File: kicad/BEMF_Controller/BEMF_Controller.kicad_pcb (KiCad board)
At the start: 2 copper layers, 164 parts, among them J1 HEADER4VALULOK, J2 HEADER6, J3 FUSE, J4 Coil_A, J5 Coil_B, J6 Coil_C, J7 Vin, Q1 C3M0280090D, Q2 C3M0280090D, Q3 C3M0280090D, Q4 C3M0280090D, Q5 C3M0280090D, Q6 C3M0280090D, U1 RASPBERRY_PICO-NO_DEBUG, U2 INA181, U3 TC1240A, U4 V_REG_78XX, U5 DGD2304, U6 DGD2304, U7 DGD2304

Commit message: reverted pcb back to original
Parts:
- removed C10, C24, C25, C26, C27, C32, C33, C34, C35, C6, C7, C8: 470uF, main:CPOL-RADIAL-5MM-10MM
- removed C13, C21, C22, C23, C28, C29, C30, C31, C36, C37, C38, C39: 1uF, Capacitor_SMD:C_1812_4532Metric
- removed C40, C41, C42: 1nF/50V, Capacitor_SMD:C_1210_3225Metric
- removed D10, D11, D12, D13, D14, D15, D16, D17, D18, D19, D20, D21, D22, D23, D24, D25, D26, D27, D28, D29, D30, D31, D32, D33, D34, D35, D36, D37, D38, D39, D40, D41, D42, D43, D44, D45, D46, D5, D6, D7, D8, D9: FSV20150V, Package_TO_SOT_SMD:TO-277A
- removed D47, D48, D51, D52, D55, D56: BZT52-B75J, main:SOD-123
- removed D49, D50, D53, D54, D57, D58: 1N4148WS, Diode_SMD:D_SOD-323
- removed J4: Coil_A, TerminalBlock_Phoenix:TerminalBlock_Phoenix_MKDS-1,5-2-5.08_1x02_P5.08mm_Horizontal
- removed J5: Coil_B, TerminalBlock_Phoenix:TerminalBlock_Phoenix_MKDS-1,5-2-5.08_1x02_P5.08mm_Horizontal
- removed J6: Coil_C, TerminalBlock_Phoenix:TerminalBlock_Phoenix_MKDS-1,5-2-5.08_1x02_P5.08mm_Horizontal
- removed J7: Vin, TerminalBlock_Phoenix:TerminalBlock_Phoenix_MKDS-1,5-2-5.08_1x02_P5.08mm_Horizontal
- removed JP1, JP2, JP3, JP4, JP5, JP6, JP7: Jumper, Jumper:SolderJumper-2_P1.3mm_Open_RoundedPad1.0x1.5mm
- removed R20, R21, R22, R23, R24, R25: 10k, Resistor_SMD:R_1210_3225Metric
- C1, C11, C12, C14, C15, C16, C17, C18, C19, C2, C20, C3: footprint Capacitor_SMD:C_1812_4532Metric -> main:1206
- C9: footprint Capacitor_SMD:C_0805_2012Metric -> main:1206
- Q1, Q2, Q3, Q4, Q5, Q6: value C3M0280090D -> MOSFET-NCHANNELTO-220-FLAT; footprint Package_TO_SOT_THT:TO-247-3_Horizontal_TabDown -> main:TO-220-FLAT
- R14, R15, R16, R17, R18, R19: value 10 -> 22; footprint Resistor_THT:R_Axial_DIN0411_L9.9mm_D3.6mm_P15.24mm_Horizontal -> main:1206
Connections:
- net /OVP_A renamed Net-(U1-GP0-Pad1)
- net /OVP_B renamed Net-(U1-GP1-Pad2)
- net /OVP_C renamed Net-(U1-GP2-Pad4)
- C9 pad 1: Net-(C9-Pad1) -> /THROTTLE
- Q1 pad 2: Net-(D9-K) -> /V_RAW
- Q1 pad 3: /SHUNT+ -> /COM_A
- Q2 pad 2: /CAP_BANK_A -> /COM_A
- Q2 pad 3: /COM_A -> /SHUNT+
- Q3 pad 2: /CAP_BANK_B -> /V_RAW
- Q4 pad 2: Net-(D41-K) -> /COM_B
- Q5 pad 2: /CAP_BANK_C -> /V_RAW
- Q6 pad 2: Net-(D45-K) -> /COM_C
- R14 pad 1: Net-(Q2-G) -> /DRV_AH
- R14 pad 2: /DRV_AH -> Net-(Q1-G)
- R15 pad 1: Net-(Q1-G) -> /DRV_AL
- R15 pad 2: /DRV_AL -> Net-(Q2-G)
- R16 pad 1: Net-(Q3-G) -> /DRV_BH
- R16 pad 2: /DRV_BH -> Net-(Q3-G)
- R17 pad 1: Net-(Q4-G) -> /DRV_BL
- R17 pad 2: /DRV_BL -> Net-(Q4-G)
- R18 pad 1: Net-(Q5-G) -> /DRV_CH
- R18 pad 2: /DRV_CH -> Net-(Q5-G)
- R19 pad 1: Net-(Q6-G) -> /DRV_CL
- R19 pad 2: /DRV_CL -> Net-(Q6-G)
- R8 pad 2: Net-(C9-Pad1) -> /THROTTLE
- U4 pad IN: Net-(J7-Pin_1) -> /V_RAW
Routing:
- net Net-(Q2-G): track 0.00 -> 39.6 mm, vias 0 -> 1
- net Net-(D9-K): track 39.6 -> 0.00 mm, vias 1 -> 0

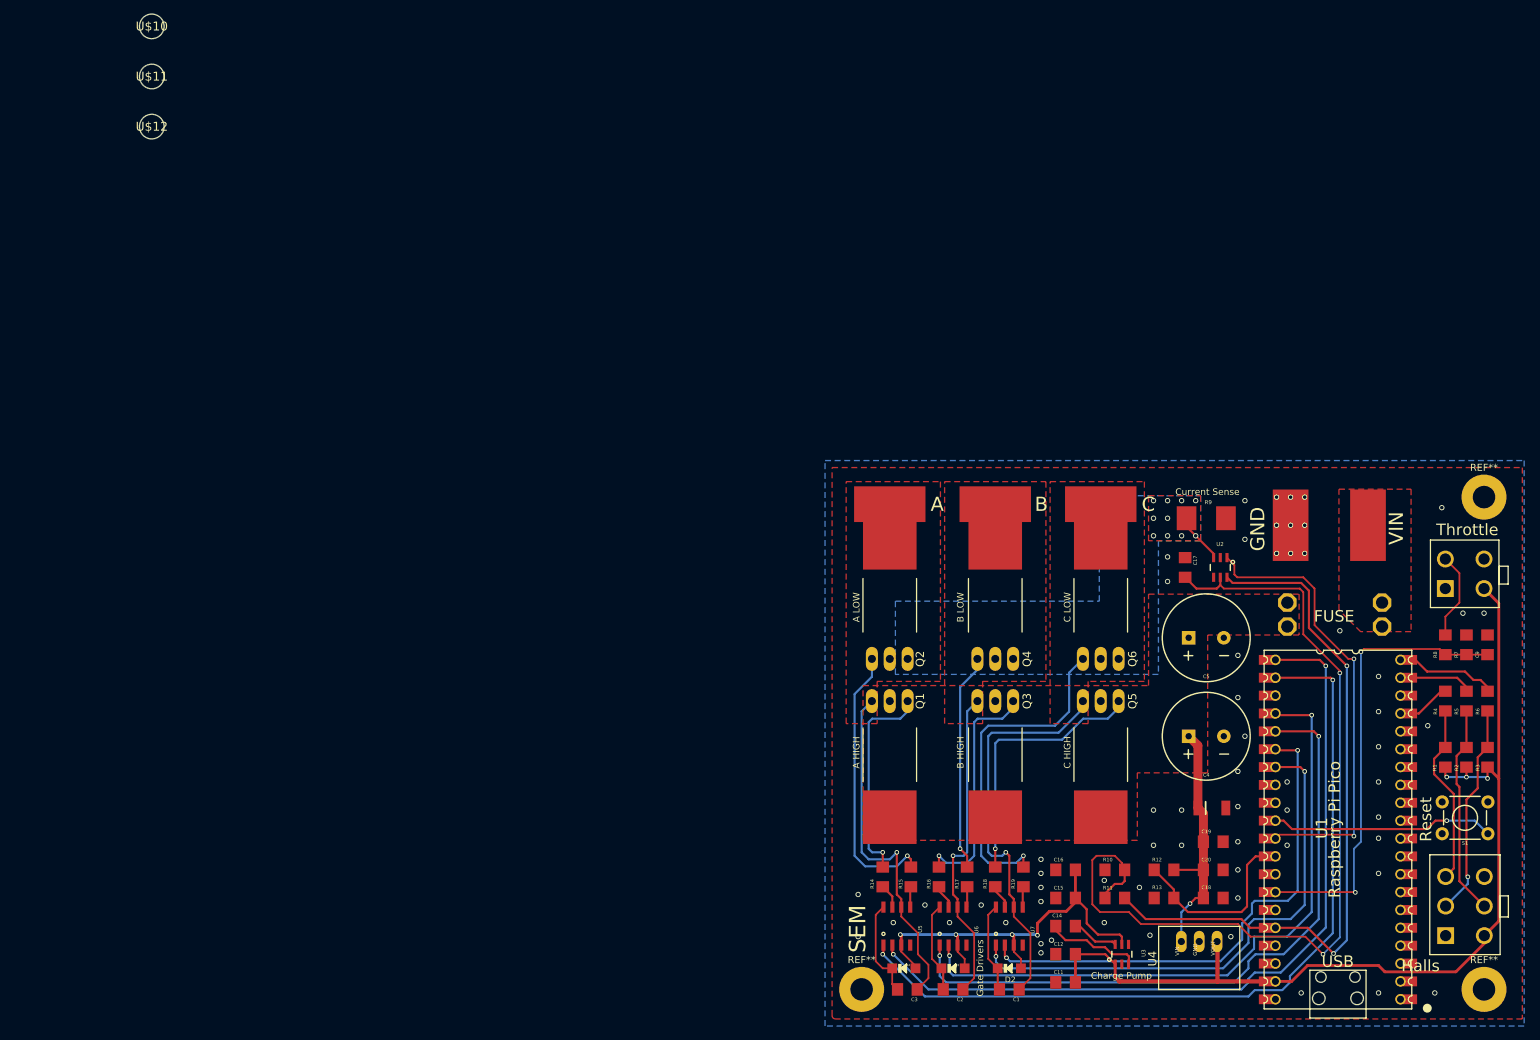
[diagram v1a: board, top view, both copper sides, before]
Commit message: Added component library
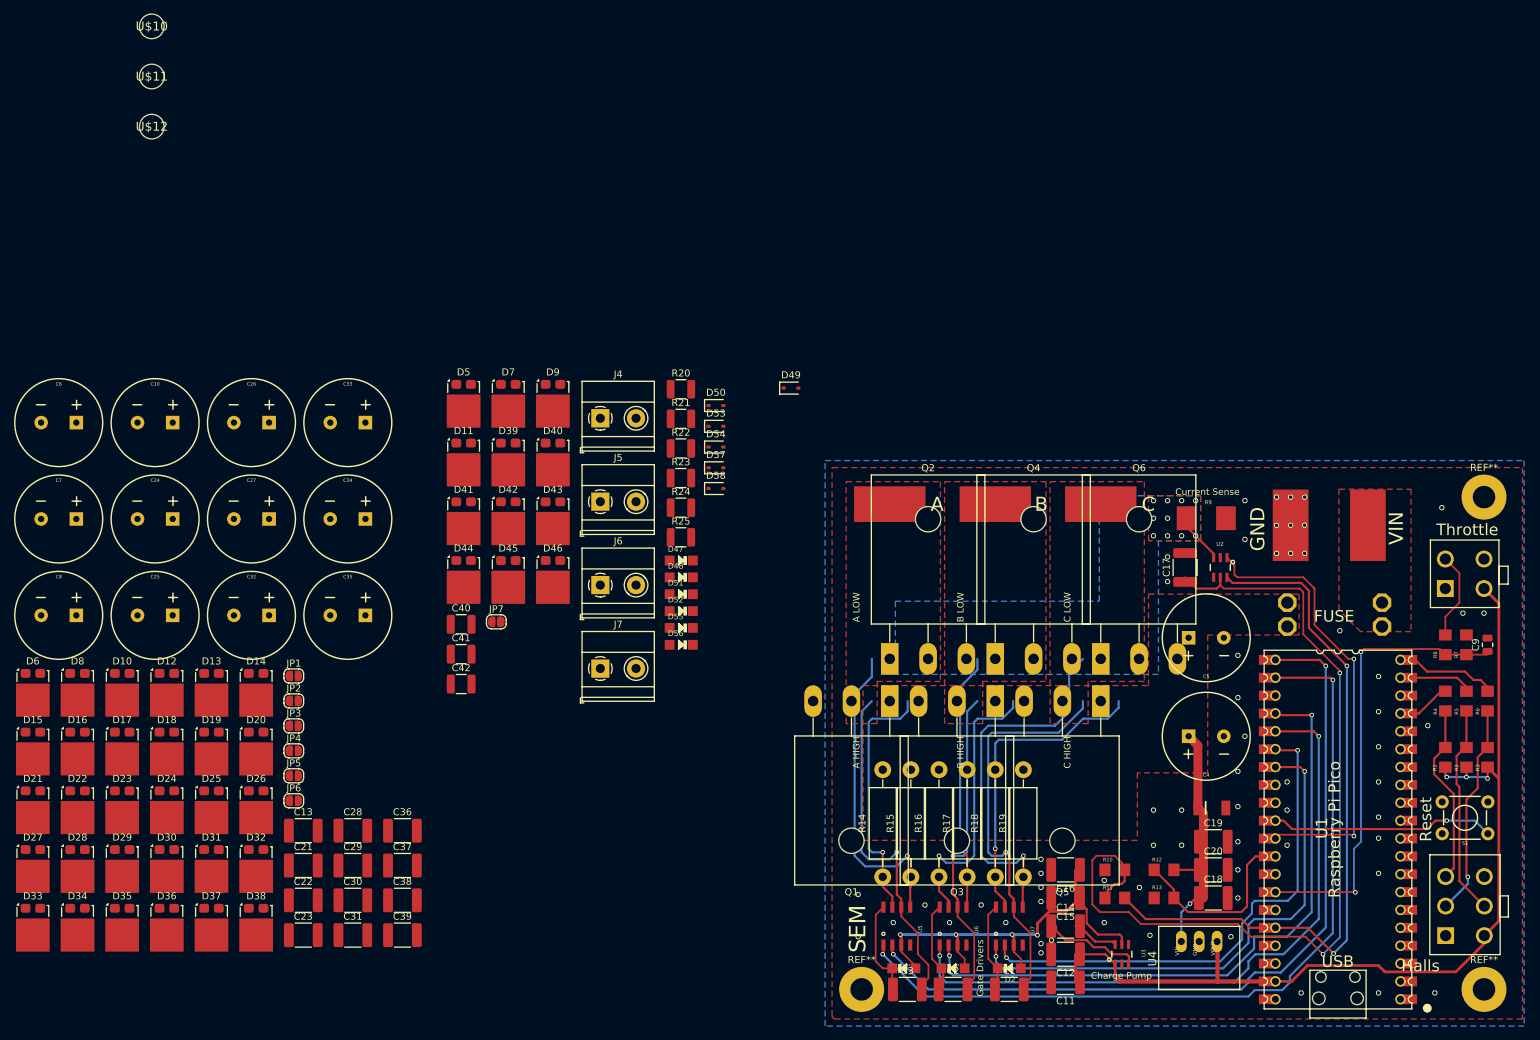
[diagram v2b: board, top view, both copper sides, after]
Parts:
- added C10: 470uF, main:CPOL-RADIAL-5MM-10MM, F.Cu at (3.53, 59.4)
- added C13: 1uF, Capacitor_SMD:C_1812_4532Metric, F.Cu at (24.6, 117.4)
- added C21: 1uF, Capacitor_SMD:C_1812_4532Metric, F.Cu at (24.6, 122.4)
- added C22: 1uF, Capacitor_SMD:C_1812_4532Metric, F.Cu at (24.6, 127.3)
- added C23: 1uF, Capacitor_SMD:C_1812_4532Metric, F.Cu at (24.6, 132.3)
- added C24: 470uF, main:CPOL-RADIAL-5MM-10MM, F.Cu at (3.53, 73.1)
- added C25: 470uF, main:CPOL-RADIAL-5MM-10MM, F.Cu at (3.53, 86.8)
- added C26: 470uF, main:CPOL-RADIAL-5MM-10MM, F.Cu at (17.2, 59.4)
- added C27: 470uF, main:CPOL-RADIAL-5MM-10MM, F.Cu at (17.2, 73.1)
- added C28: 1uF, Capacitor_SMD:C_1812_4532Metric, F.Cu at (31.7, 117.4)
- added C29: 1uF, Capacitor_SMD:C_1812_4532Metric, F.Cu at (31.7, 122.4)
- added C30: 1uF, Capacitor_SMD:C_1812_4532Metric, F.Cu at (31.7, 127.3)
- added C31: 1uF, Capacitor_SMD:C_1812_4532Metric, F.Cu at (31.7, 132.3)
- added C32: 470uF, main:CPOL-RADIAL-5MM-10MM, F.Cu at (17.2, 86.8)
- added C33: 470uF, main:CPOL-RADIAL-5MM-10MM, F.Cu at (30.9, 59.4)
- added C34: 470uF, main:CPOL-RADIAL-5MM-10MM, F.Cu at (30.9, 73.1)
- added C35: 470uF, main:CPOL-RADIAL-5MM-10MM, F.Cu at (30.9, 86.8)
- added C36: 1uF, Capacitor_SMD:C_1812_4532Metric, F.Cu at (38.7, 117.4)
- added C37: 1uF, Capacitor_SMD:C_1812_4532Metric, F.Cu at (38.7, 122.4)
- added C38: 1uF, Capacitor_SMD:C_1812_4532Metric, F.Cu at (38.7, 127.3)
- added C39: 1uF, Capacitor_SMD:C_1812_4532Metric, F.Cu at (38.7, 132.3)
- added C40: 1nF/50V, Capacitor_SMD:C_1210_3225Metric, F.Cu at (47.1, 88.1)
- added C41: 1nF/50V, Capacitor_SMD:C_1210_3225Metric, F.Cu at (47.1, 92.3)
- added C42: 1nF/50V, Capacitor_SMD:C_1210_3225Metric, F.Cu at (47.1, 96.6)
- added C6: 470uF, main:CPOL-RADIAL-5MM-10MM, F.Cu at (-10.2, 59.4)
- added C7: 470uF, main:CPOL-RADIAL-5MM-10MM, F.Cu at (-10.2, 73.1)
- added C8: 470uF, main:CPOL-RADIAL-5MM-10MM, F.Cu at (-10.2, 86.8)
- added D10: FSV20150V, Package_TO_SOT_SMD:TO-277A, F.Cu at (-1.15, 97.8)
- added D11: FSV20150V, Package_TO_SOT_SMD:TO-277A, F.Cu at (47.4, 65.1)
- added D12: FSV20150V, Package_TO_SOT_SMD:TO-277A, F.Cu at (5.20, 97.8)
- added D13: FSV20150V, Package_TO_SOT_SMD:TO-277A, F.Cu at (11.6, 97.8)
- added D14: FSV20150V, Package_TO_SOT_SMD:TO-277A, F.Cu at (17.9, 97.8)
- added D15: FSV20150V, Package_TO_SOT_SMD:TO-277A, F.Cu at (-13.8, 106.2)
- added D16: FSV20150V, Package_TO_SOT_SMD:TO-277A, F.Cu at (-7.50, 106.2)
- added D17: FSV20150V, Package_TO_SOT_SMD:TO-277A, F.Cu at (-1.15, 106.2)
- added D18: FSV20150V, Package_TO_SOT_SMD:TO-277A, F.Cu at (5.20, 106.2)
- added D19: FSV20150V, Package_TO_SOT_SMD:TO-277A, F.Cu at (11.6, 106.2)
- added D20: FSV20150V, Package_TO_SOT_SMD:TO-277A, F.Cu at (17.9, 106.2)
- added D21: FSV20150V, Package_TO_SOT_SMD:TO-277A, F.Cu at (-13.8, 114.5)
- added D22: FSV20150V, Package_TO_SOT_SMD:TO-277A, F.Cu at (-7.50, 114.5)
- added D23: FSV20150V, Package_TO_SOT_SMD:TO-277A, F.Cu at (-1.15, 114.5)
- added D24: FSV20150V, Package_TO_SOT_SMD:TO-277A, F.Cu at (5.20, 114.5)
- added D25: FSV20150V, Package_TO_SOT_SMD:TO-277A, F.Cu at (11.6, 114.5)
- added D26: FSV20150V, Package_TO_SOT_SMD:TO-277A, F.Cu at (17.9, 114.5)
- added D27: FSV20150V, Package_TO_SOT_SMD:TO-277A, F.Cu at (-13.8, 122.9)
- added D28: FSV20150V, Package_TO_SOT_SMD:TO-277A, F.Cu at (-7.50, 122.9)
- added D29: FSV20150V, Package_TO_SOT_SMD:TO-277A, F.Cu at (-1.15, 122.9)
- added D30: FSV20150V, Package_TO_SOT_SMD:TO-277A, F.Cu at (5.20, 122.9)
- added D31: FSV20150V, Package_TO_SOT_SMD:TO-277A, F.Cu at (11.6, 122.9)
- added D32: FSV20150V, Package_TO_SOT_SMD:TO-277A, F.Cu at (17.9, 122.9)
- added D33: FSV20150V, Package_TO_SOT_SMD:TO-277A, F.Cu at (-13.8, 131.2)
- added D34: FSV20150V, Package_TO_SOT_SMD:TO-277A, F.Cu at (-7.50, 131.2)
- added D35: FSV20150V, Package_TO_SOT_SMD:TO-277A, F.Cu at (-1.15, 131.2)
- added D36: FSV20150V, Package_TO_SOT_SMD:TO-277A, F.Cu at (5.20, 131.2)
- added D37: FSV20150V, Package_TO_SOT_SMD:TO-277A, F.Cu at (11.6, 131.2)
- added D38: FSV20150V, Package_TO_SOT_SMD:TO-277A, F.Cu at (17.9, 131.2)
- added D39: FSV20150V, Package_TO_SOT_SMD:TO-277A, F.Cu at (53.8, 65.1)
- added D40: FSV20150V, Package_TO_SOT_SMD:TO-277A, F.Cu at (60.1, 65.1)
- added D41: FSV20150V, Package_TO_SOT_SMD:TO-277A, F.Cu at (47.4, 73.4)
- added D42: FSV20150V, Package_TO_SOT_SMD:TO-277A, F.Cu at (53.8, 73.4)
- added D43: FSV20150V, Package_TO_SOT_SMD:TO-277A, F.Cu at (60.1, 73.4)
- added D44: FSV20150V, Package_TO_SOT_SMD:TO-277A, F.Cu at (47.4, 81.8)
- added D45: FSV20150V, Package_TO_SOT_SMD:TO-277A, F.Cu at (53.8, 81.8)
- added D46: FSV20150V, Package_TO_SOT_SMD:TO-277A, F.Cu at (60.1, 81.8)
- added D47: BZT52-B75J, main:SOD-123, F.Cu at (78.3, 79.0)
- added D48: BZT52-B75J, main:SOD-123, F.Cu at (78.3, 81.4)
- added D49: 1N4148WS, Diode_SMD:D_SOD-323, F.Cu at (94.0, 54.5)
- added D5: FSV20150V, Package_TO_SOT_SMD:TO-277A, F.Cu at (47.4, 56.7)
- added D50: 1N4148WS, Diode_SMD:D_SOD-323, F.Cu at (83.3, 57.0)
- added D51: BZT52-B75J, main:SOD-123, F.Cu at (78.3, 83.8)
- added D52: BZT52-B75J, main:SOD-123, F.Cu at (78.3, 86.2)
- added D53: 1N4148WS, Diode_SMD:D_SOD-323, F.Cu at (83.3, 59.9)
- added D54: 1N4148WS, Diode_SMD:D_SOD-323, F.Cu at (83.3, 62.9)
- added D55: BZT52-B75J, main:SOD-123, F.Cu at (78.3, 88.6)
- added D56: BZT52-B75J, main:SOD-123, F.Cu at (78.3, 91.0)
- added D57: 1N4148WS, Diode_SMD:D_SOD-323, F.Cu at (83.3, 65.8)
- added D58: 1N4148WS, Diode_SMD:D_SOD-323, F.Cu at (83.3, 68.8)
- added D6: FSV20150V, Package_TO_SOT_SMD:TO-277A, F.Cu at (-13.8, 97.8)
- added D7: FSV20150V, Package_TO_SOT_SMD:TO-277A, F.Cu at (53.8, 56.7)
- added D8: FSV20150V, Package_TO_SOT_SMD:TO-277A, F.Cu at (-7.50, 97.8)
- added D9: FSV20150V, Package_TO_SOT_SMD:TO-277A, F.Cu at (60.1, 56.7)
- added J4: Coil_A, TerminalBlock_Phoenix:TerminalBlock_Phoenix_MKDS-1,5-2-5.08_1x02_P5.08mm_Horizontal, F.Cu at (66.8, 58.8)
- added J5: Coil_B, TerminalBlock_Phoenix:TerminalBlock_Phoenix_MKDS-1,5-2-5.08_1x02_P5.08mm_Horizontal, F.Cu at (66.8, 70.7)
- added J6: Coil_C, TerminalBlock_Phoenix:TerminalBlock_Phoenix_MKDS-1,5-2-5.08_1x02_P5.08mm_Horizontal, F.Cu at (66.8, 82.5)
- added J7: Vin, TerminalBlock_Phoenix:TerminalBlock_Phoenix_MKDS-1,5-2-5.08_1x02_P5.08mm_Horizontal, F.Cu at (66.8, 94.4)
- added JP1: Jumper, Jumper:SolderJumper-2_P1.3mm_Open_RoundedPad1.0x1.5mm, F.Cu at (23.3, 95.4)
- added JP2: Jumper, Jumper:SolderJumper-2_P1.3mm_Open_RoundedPad1.0x1.5mm, F.Cu at (23.3, 99.0)
- added JP3: Jumper, Jumper:SolderJumper-2_P1.3mm_Open_RoundedPad1.0x1.5mm, F.Cu at (23.3, 102.5)
- added JP4: Jumper, Jumper:SolderJumper-2_P1.3mm_Open_RoundedPad1.0x1.5mm, F.Cu at (23.3, 106.1)
- added JP5: Jumper, Jumper:SolderJumper-2_P1.3mm_Open_RoundedPad1.0x1.5mm, F.Cu at (23.3, 109.6)
- added JP6: Jumper, Jumper:SolderJumper-2_P1.3mm_Open_RoundedPad1.0x1.5mm, F.Cu at (23.3, 113.2)
- added JP7: Jumper, Jumper:SolderJumper-2_P1.3mm_Open_RoundedPad1.0x1.5mm, F.Cu at (52.1, 87.7)
- added R20: 10k, Resistor_SMD:R_1210_3225Metric, F.Cu at (78.3, 54.7)
- added R21: 10k, Resistor_SMD:R_1210_3225Metric, F.Cu at (78.3, 58.9)
- added R22: 10k, Resistor_SMD:R_1210_3225Metric, F.Cu at (78.3, 63.1)
- added R23: 10k, Resistor_SMD:R_1210_3225Metric, F.Cu at (78.3, 67.3)
- added R24: 10k, Resistor_SMD:R_1210_3225Metric, F.Cu at (78.3, 71.5)
- added R25: 10k, Resistor_SMD:R_1210_3225Metric, F.Cu at (78.3, 75.7)
- C1, C11, C12, C14, C15, C16, C17, C18, C19, C2, C20, C3: footprint main:1206 -> Capacitor_SMD:C_1812_4532Metric
- C9: footprint main:1206 -> Capacitor_SMD:C_0805_2012Metric
- Q1, Q2, Q3, Q4, Q5, Q6: value MOSFET-NCHANNELTO-220-FLAT -> C3M0280090D; footprint main:TO-220-FLAT -> Package_TO_SOT_THT:TO-247-3_Horizontal_TabDown
- R14, R15, R16, R17, R18, R19: value 22 -> 10; footprint main:1206 -> Resistor_THT:R_Axial_DIN0411_L9.9mm_D3.6mm_P15.24mm_Horizontal
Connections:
- net Net-(U1-GP0-Pad1) renamed /OVP_A
- net Net-(U1-GP1-Pad2) renamed /OVP_B
- net Net-(U1-GP2-Pad4) renamed /OVP_C
- C9 pad 1: /THROTTLE -> Net-(C9-Pad1)
- Q1 pad 2: /V_RAW -> Net-(D9-K)
- Q1 pad 3: /COM_A -> /SHUNT+
- Q2 pad 2: /COM_A -> /CAP_BANK_A
- Q2 pad 3: /SHUNT+ -> /COM_A
- Q3 pad 2: /V_RAW -> /CAP_BANK_B
- Q4 pad 2: /COM_B -> Net-(D41-K)
- Q5 pad 2: /V_RAW -> /CAP_BANK_C
- Q6 pad 2: /COM_C -> Net-(D45-K)
- R14 pad 1: /DRV_AH -> Net-(Q2-G)
- R14 pad 2: Net-(Q1-G) -> /DRV_AH
- R15 pad 1: /DRV_AL -> Net-(Q1-G)
- R15 pad 2: Net-(Q2-G) -> /DRV_AL
- R16 pad 1: /DRV_BH -> Net-(Q3-G)
- R16 pad 2: Net-(Q3-G) -> /DRV_BH
- R17 pad 1: /DRV_BL -> Net-(Q4-G)
- R17 pad 2: Net-(Q4-G) -> /DRV_BL
- R18 pad 1: /DRV_CH -> Net-(Q5-G)
- R18 pad 2: Net-(Q5-G) -> /DRV_CH
- R19 pad 1: /DRV_CL -> Net-(Q6-G)
- R19 pad 2: Net-(Q6-G) -> /DRV_CL
- R8 pad 2: /THROTTLE -> Net-(C9-Pad1)
- U4 pad IN: /V_RAW -> Net-(J7-Pin_1)
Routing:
- net Net-(Q2-G): track 39.6 -> 0.00 mm, vias 1 -> 0
- net Net-(D9-K): track 0.00 -> 39.6 mm, vias 0 -> 1
